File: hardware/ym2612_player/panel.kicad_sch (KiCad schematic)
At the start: 21 parts, among them J5 LCD (I2C backpack: GND, VCC, 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, Q1 BSS138, Q2 BSS138, SW1 Play (red cap), SW2 Stop, SW3 Left, SW4 Right, SW5 Edit, SW6 Exit, SW7 Write, SW8 Data knob

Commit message: Rev A PCB layout and PCBWay files
Board is 240 x 120 mm, 2 layers, placed by tools/layout.py and routed with
Freerouting (tools/route.py). DRC in KiCad 10: 0 errors, 0 unconnected,
matches the schematic. Adds Gerbers, BOM and placement (CPL) files for a
PCBWay turnkey order, and a top-view picture.

Also: volume slider moves off the board onto a 6-pin JST XH plug (J4), and
the Pico Plus 2 footprint now has its pads and outline in the right place.

Co-Authored-By: Claude Opus 5.5 (1M context) <noreply@anthropic.com>
Claude-Session: https://claude.ai/code/session_01JeM5NcWqyQVA3DixJkw6Wg
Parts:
- removed C38: 100nF, Capacitor_SMD:C_0603_1608Metric, symbol Device:C
- added SW1: Play (red cap), Button_Switch_THT:SW_PUSH-12mm, symbol Switch:SW_Push
- C35: renamed from R50; value 10k -> 10nF; footprint Resistor_SMD:R_0603_1608Metric -> Capacitor_SMD:C_0603_1608Metric; symbol Device:R -> Device:C; Spec 1%, 0603 -> X7R, 16V
- C37: renamed from J5; value LCD (I2C backpack: GND, VCC, SDA, SCL) -> 10uF; footprint Connector_JST:JST_XH_B4B-XH-A_1x04_P2.50mm_Vertical -> Capacitor_SMD:C_0805_2012Metric; symbol Connector_Generic:Conn_01x04 -> Device:C; MPN B4B-XH-A(LF)(SN) -> (none); Spec JST XH 4-pin header -> X5R, 10V, 0805
- C38: renamed from C37; value 10uF -> 100nF; footprint Capacitor_SMD:C_0805_2012Metric -> Capacitor_SMD:C_0603_1608Metric; Spec X5R, 10V, 0805 -> X7R, 16V
- J6: renamed from R54; value 4.7k -> LCD (I2C backpack: GND, VCC, SDA, SCL); footprint Resistor_SMD:R_0603_1608Metric -> Connector_JST:JST_XH_B4B-XH-A_1x04_P2.50mm_Vertical; symbol Device:R -> Connector_Generic:Conn_01x04; MPN (none) -> B4B-XH-A(LF)(SN); Spec 1%, 0603 -> JST XH 4-pin header
- Q1: renamed from C36; value 10nF -> BSS138; footprint Capacitor_SMD:C_0603_1608Metric -> Package_TO_SOT_SMD:SOT-23; symbol Device:C -> Transistor_FET:BSS138; MPN (none) -> BSS138; Spec X7R, 16V -> N-MOSFET, SOT-23
- Q2: renamed from R52; value 4.7k -> BSS138; footprint Resistor_SMD:R_0603_1608Metric -> Package_TO_SOT_SMD:SOT-23; symbol Device:R -> Transistor_FET:BSS138; MPN (none) -> BSS138; Spec 1%, 0603 -> N-MOSFET, SOT-23
- R49: renamed from SW8; value Data knob -> 10k; footprint Rotary_Encoder:RotaryEncoder_Alps_EC11E_Vertical_H20mm -> Resistor_SMD:R_0603_1608Metric; symbol Device:RotaryEncoder -> Device:R; MPN PEC11R-4215F-N0024 -> (none); Spec Bourns 24-step encoder, no push switch, 15 mm shaft (EC11 f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 -> 1%, 0603
- R51: renamed from Q1; value BSS138 -> 4.7k; footprint Package_TO_SOT_SMD:SOT-23 -> Resistor_SMD:R_0603_1608Metric; symbol Transistor_FET:BSS138 -> Device:R; MPN BSS138 -> (none); Spec N-MOSFET, SOT-23 -> 1%, 0603
- R53: renamed from Q2; value BSS138 -> 4.7k; footprint Package_TO_SOT_SMD:SOT-23 -> Resistor_SMD:R_0603_1608Metric; symbol Transistor_FET:BSS138 -> Device:R; MPN BSS138 -> (none); Spec N-MOSFET, SOT-23 -> 1%, 0603
- SW2: renamed from SW1; value Play (red cap) -> Stop
- SW3: renamed from SW2; value Stop -> Left
- SW4: renamed from SW3; value Left -> Right
- SW5: renamed from SW4; value Right -> Edit
- SW6: renamed from SW5; value Edit -> Exit
- SW7: renamed from SW6; value Exit -> Write
- SW8: renamed from SW7; value Write -> Data knob; footprint Button_Switch_THT:SW_PUSH-12mm -> Rotary_Encoder:RotaryEncoder_Alps_EC11E_Vertical_H20mm; symbol Switch:SW_Push -> Device:RotaryEncoder; MPN B3F-4055 -> PEC11R-4215F-N0024; Spec Omron 12 mm tactile switch, 7.3 mm tall, with a B32-series 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 -> Bourns 24-step encoder, no push switch, 15 mm shaft (EC11 f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
- renumbered C35 to C36, R49 to R50, R51 to R52, R53 to R54
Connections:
- net +3V3: now also Q1.1 (G), Q2.1 (G), R49.1; no longer C35.1, R52.1, R54.1
- net +5V: now also C37.1, J6.2 (Pin_2), R52.1, R54.1; no longer C37.2 (Pin_2), J6.1, Q2.1
- net BTN_EDIT: now also SW5.1; no longer SW6.1
- net BTN_EXIT: now also SW6.1; no longer SW7.1
- net BTN_LEFT: now also SW3.1; no longer SW4.1
- net BTN_PLAY: now also SW1.1; no longer SW2.1
- net BTN_RIGHT: now also SW4.1; no longer SW5.1
- net BTN_STOP: now also SW2.1; no longer SW3.1
- net BTN_WRITE: now also SW7.1; no longer SW8.1
- net ENC_A: now also C35.1, R49.2, SW8.A; no longer C36.1, R49.A, R50.2
- net ENC_B: now also C36.1, R50.2, SW8.B; no longer C35.2, Q1.1, R49.B
- net GND: now also C35.2, C37.2, J6.1 (Pin_1), SW8.C, SW1.2; no longer C37.1 (Pin_1), Q1.2, R49.C, SW8.2
- net I2C_SCL: now also Q2.2 (S); no longer R54.2
- net I2C_SDA: now also Q1.2 (S); no longer R52.2
- net LCD_SCL: now also J6.4 (Pin_4), Q2.3 (D), R54.2; no longer C37.4 (Pin_4), J6.2, R53.3 (D)
- net LCD_SDA: now also J6.3 (Pin_3), Q1.3 (D), R52.2; no longer C37.3 (Pin_3), Q2.2, R51.3 (D)
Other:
- moved on the sheet: C36, C38, R50, R52, R54, SW2, SW3, SW4, SW5, SW6, SW7

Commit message: Apply the Rev A fix register: decoupling, single ground, A.VCC filter, TPA6132A2
Schematic
- YM2612 A.VCC (pin 22) gets its own 10 ohm + 220 uF + 100 nF filter.
- /IC, A0, A1 pull-downs 10k -> 4.7k (RP2350 erratum E9).
- Headphone amp: NJM4556A replaced by a TPA6132A2 at -6 dB, no output caps,
  enabled by GP12 (HP_EN, 4.7k pull-down) so power-up doesn't pop.
- 47 uF electrolytic damps the L1/C4 resonance before the LP5907.
- GNDA merged into GND; NT1 removed. Four M3 holes for the LCD standoffs.
- Ferrite label 220R@100MHz to match BLM18PG221SN1D; C15/C22 spec X7R 50V;
  LED lead note for PCBWay.
- Pico Plus 2 and its headers marked do-not-fit (Joey supplies them);
  sockets are Sullins PPTC201LFBN-RC.

Layout
- Decoupling caps placed at the pin they serve (design.NEAR), 2-7 mm instead
  of 16-70 mm.
- One solid GND plane on both layers plus 332 stitching vias (tools/stitch.py).
- J6 moved out from under the LCD backpack; encoder moved below the LCD so
  the knob clears it.
- Re-routed with Freerouting; KiCad 7 DRC: 0 errors, 0 unconnected.

Co-Authored-By: Claude Opus 5.5 (1M context) <noreply@anthropic.com>
Claude-Session: https://claude.ai/code/session_01T6y8roX1LzS9uTuKVQBe9X
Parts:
- removed SW1: Play (red cap), Button_Switch_THT:SW_PUSH-12mm, symbol Switch:SW_Push
- removed SW2: Stop, Button_Switch_THT:SW_PUSH-12mm, symbol Switch:SW_Push
- added C41: 10uF, Capacitor_SMD:C_0805_2012Metric, symbol Device:C
- added C42: 100nF, Capacitor_SMD:C_0603_1608Metric, symbol Device:C
- C39: renamed from Q1; value BSS138 -> 10nF; footprint Package_TO_SOT_SMD:SOT-23 -> Capacitor_SMD:C_0603_1608Metric; symbol Transistor_FET:BSS138 -> Device:C; MPN BSS138 -> (none); Spec N-MOSFET, SOT-23 -> X7R, 16V
- C40: renamed from R51; value 4.7k -> 10nF; footprint Resistor_SMD:R_0603_1608Metric -> Capacitor_SMD:C_0603_1608Metric; symbol Device:R -> Device:C; Spec 1%, 0603 -> X7R, 16V
- J6: renamed from C38; value 100nF -> LCD (I2C backpack: GND, VCC, SDA, SCL); footprint Capacitor_SMD:C_0603_1608Metric -> Connector_JST:JST_XH_B4B-XH-A_1x04_P2.50mm_Vertical; symbol Device:C -> Connector_Generic:Conn_01x04; MPN (none) -> B4B-XH-A(LF)(SN); Spec X7R, 16V -> JST XH 4-pin header
- Q1: renamed from R52; value 4.7k -> BSS138; footprint Resistor_SMD:R_0603_1608Metric -> Package_TO_SOT_SMD:SOT-23; symbol Device:R -> Transistor_FET:BSS138; MPN (none) -> BSS138; Spec 1%, 0603 -> N-MOSFET, SOT-23
- Q2: renamed from R54; value 4.7k -> BSS138; footprint Resistor_SMD:R_0603_1608Metric -> Package_TO_SOT_SMD:SOT-23; symbol Device:R -> Transistor_FET:BSS138; MPN (none) -> BSS138; Spec 1%, 0603 -> N-MOSFET, SOT-23
- R45: renamed from C35; value 10nF -> 10k; footprint Capacitor_SMD:C_0603_1608Metric -> Resistor_SMD:R_0603_1608Metric; symbol Device:C -> Device:R; Spec X7R, 16V -> 1%, 0603
- R46: renamed from C36; value 10nF -> 10k; footprint Capacitor_SMD:C_0603_1608Metric -> Resistor_SMD:R_0603_1608Metric; symbol Device:C -> Device:R; Spec X7R, 16V -> 1%, 0603
- R47: renamed from Q2; value BSS138 -> 4.7k; footprint Package_TO_SOT_SMD:SOT-23 -> Resistor_SMD:R_0603_1608Metric; symbol Transistor_FET:BSS138 -> Device:R; MPN BSS138 -> (none); Spec N-MOSFET, SOT-23 -> 1%, 0603
- R49: renamed from J6; value LCD (I2C backpack: GND, VCC, SDA, SCL) -> 4.7k; footprint Connector_JST:JST_XH_B4B-XH-A_1x04_P2.50mm_Vertical -> Resistor_SMD:R_0603_1608Metric; symbol Connector_Generic:Conn_01x04 -> Device:R; MPN B4B-XH-A(LF)(SN) -> (none); Spec JST XH 4-pin header -> 1%, 0603
- R50: renamed from C37; value 10uF -> 4.7k; footprint Capacitor_SMD:C_0805_2012Metric -> Resistor_SMD:R_0603_1608Metric; symbol Device:C -> Device:R; Spec X5R, 10V, 0805 -> 1%, 0603
- SW1: renamed from SW3; value Left -> Play (red cap)
- SW2: renamed from SW4; value Right -> Stop
- SW3: renamed from SW5; value Edit -> Left
- SW4: renamed from SW6; value Exit -> Right
- SW5: renamed from SW7; value Write -> Edit
- SW6: renamed from SW8; value Data knob -> Exit; footprint Rotary_Encoder:RotaryEncoder_Alps_EC11E_Vertical_H20mm -> Button_Switch_THT:SW_PUSH-12mm; symbol Device:RotaryEncoder -> Switch:SW_Push; MPN PEC11R-4215F-N0024 -> B3F-4055; Spec Bourns 24-step encoder, no push switch, 15 mm shaft (EC11 f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 -> Omron 12 mm tactile switch, 7.3 mm tall, with a B32-series 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
- SW7: renamed from R49; value 10k -> Write; footprint Resistor_SMD:R_0603_1608Metric -> Button_Switch_THT:SW_PUSH-12mm; symbol Device:R -> Switch:SW_Push; MPN (none) -> B3F-4055; Spec 1%, 0603 -> Omron 12 mm tactile switch, 7.3 mm tall, with a B32-series 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
- SW8: renamed from R50; value 10k -> Data knob; footprint Resistor_SMD:R_0603_1608Metric -> Rotary_Encoder:RotaryEncoder_Alps_EC11E_Vertical_H20mm; symbol Device:R -> Device:RotaryEncoder; MPN (none) -> PEC11R-4215F-N0024; Spec 1%, 0603 -> Bourns 24-step encoder, no push switch, 15 mm shaft (EC11 f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
- renumbered R53 to R48
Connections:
- net +3V3: now also Q1.1 (G), Q2.1 (G), R45.1, R46.1, R49.1; no longer C39.1 (G), C40.1, R48.1, SW7.1, SW8.1
- net +5V: now also J6.2 (Pin_2), R48.1, C41.1, C42.1; no longer J6.1, Q1.1, Q2.1, R49.2 (Pin_2)
- net BTN_EDIT: now also SW5.1; no longer SW3.1
- net BTN_EXIT: now also SW6.1; no longer SW4.1
- net BTN_LEFT: now also SW3.1; no longer SW1.1
- net BTN_PLAY: now also SW1.1
- net BTN_RIGHT: now also SW4.1; no longer SW2.1
- net BTN_STOP: now also SW2.1
- net BTN_WRITE: now also SW7.1; no longer SW5.1
- net ENC_A: now also C39.1, R45.2, SW8.A; no longer R45.1, SW6.A, SW7.2
- net ENC_B: now also C40.1, R46.2, SW8.B; no longer R46.1, SW6.B, SW8.2
- net GND: now also C39.2, C40.2, J6.1 (Pin_1), SW6.2, SW7.2, SW8.C, C41.2, C42.2; no longer J6.2, R45.2, R46.2, R49.1 (Pin_1), R50.2, SW6.C
- net I2C_SCL: now also Q2.2 (S), R49.2; no longer R47.2 (S), R48.2
- net I2C_SDA: now also Q1.2 (S), R47.2; no longer C39.2 (S), C40.2
- net LCD_SCL: now also J6.4 (Pin_4), Q2.3 (D), R50.2; no longer Q2.2, R47.3 (D), R49.4 (Pin_4)
- net LCD_SDA: now also J6.3 (Pin_3), Q1.3 (D), R48.2; no longer C39.3 (D), Q1.2, R49.3 (Pin_3)
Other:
- moved on the sheet: R48, SW1, SW2, SW3, SW4, SW5

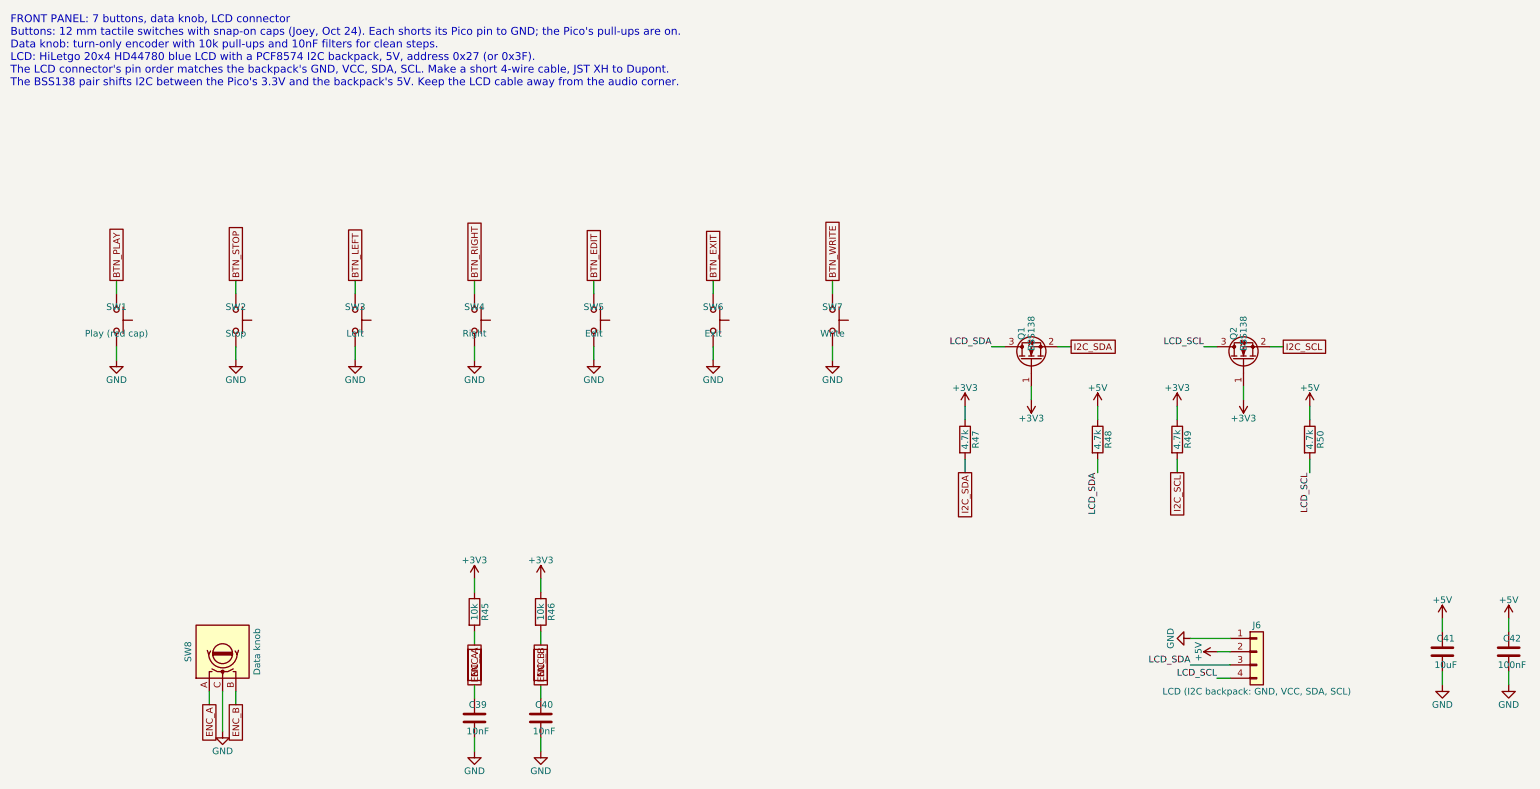
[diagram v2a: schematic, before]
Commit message: Schematic: draw real wires between parts instead of name tags
tools/wires.py routes each page's nets on the 1.27 mm grid around part bodies and text.
Power pins keep power symbols (neighbouring pins share one), signals that leave a page get
one global label, and the netlist check still matches design.py exactly (0 mismatches).
Sound chip and audio pages re-laid out so the wiring reads left to right; title blocks say Rev B.

Co-Authored-By: Claude Opus 5.5 <noreply@anthropic.com>
Claude-Session: https://claude.ai/code/session_01TDTDVidYRoyJdUGgsyVTSw
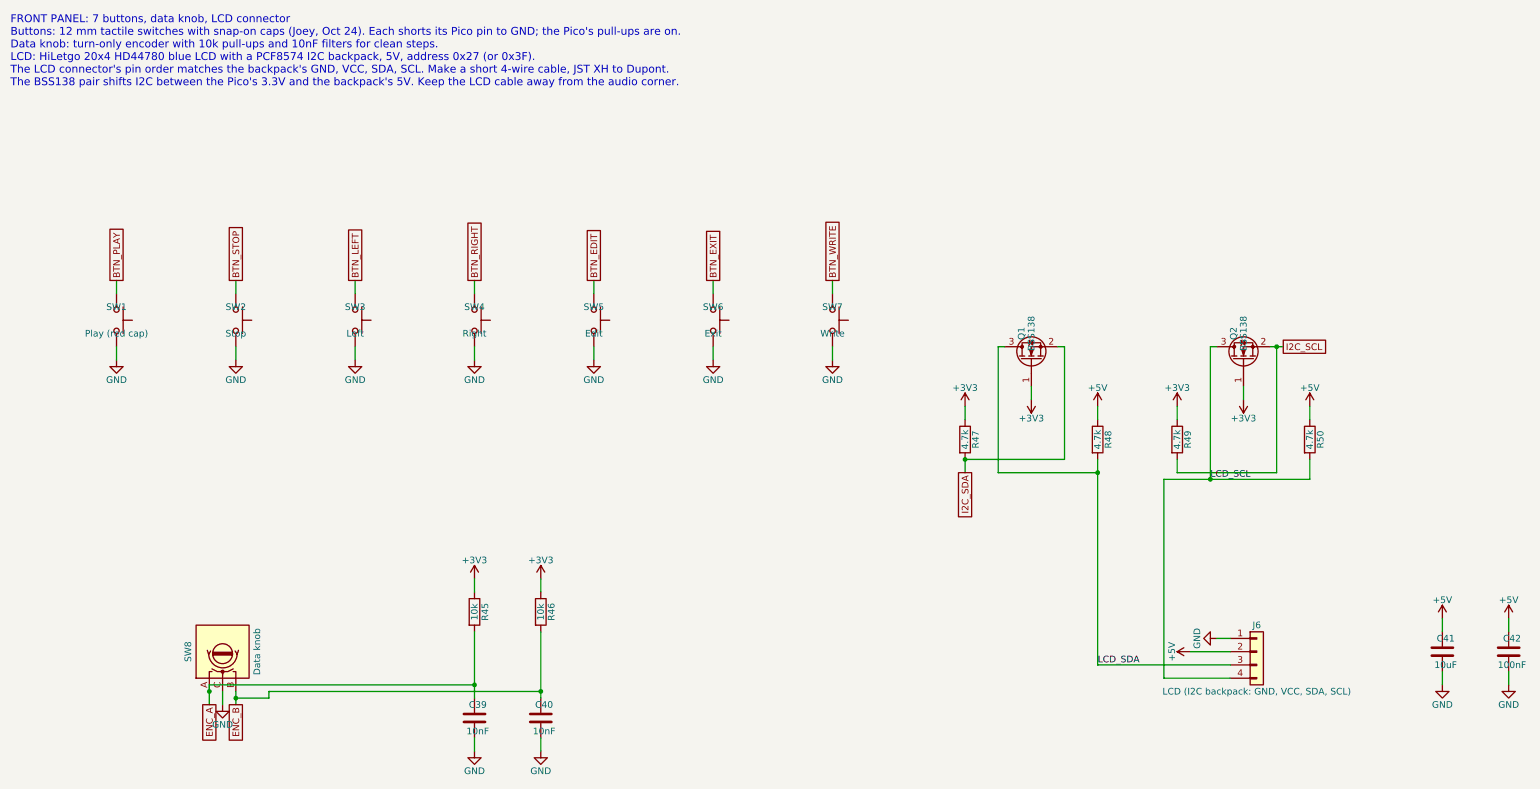
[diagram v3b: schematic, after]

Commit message: Schematic: PWR_FLAG on YM_AVCC (KiCad 10 ERC: A.VCC is fed through R21)
Co-Authored-By: Claude Opus 5.5 <noreply@anthropic.com>
Claude-Session: https://claude.ai/code/session_01TDTDVidYRoyJdUGgsyVTSw
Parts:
- removed SW1: Play (red cap), Button_Switch_THT:SW_PUSH-12mm, symbol Switch:SW_Push
- added C42: 100nF, Capacitor_SMD:C_0603_1608Metric, symbol Device:C
- C40: renamed from Q1; value BSS138 -> 10nF; footprint Package_TO_SOT_SMD:SOT-23 -> Capacitor_SMD:C_0603_1608Metric; symbol Transistor_FET:BSS138 -> Device:C; MPN BSS138 -> (none); Spec N-MOSFET, SOT-23 -> X7R, 16V
- C41: renamed from C42; value 100nF -> 10uF; footprint Capacitor_SMD:C_0603_1608Metric -> Capacitor_SMD:C_0805_2012Metric; Spec X7R, 16V -> X5R, 10V, 0805
- J6: renamed from C41; value 10uF -> LCD (I2C backpack: GND, VCC, SDA, SCL); footprint Capacitor_SMD:C_0805_2012Metric -> Connector_JST:JST_XH_B4B-XH-A_1x04_P2.50mm_Vertical; symbol Device:C -> Connector_Generic:Conn_01x04; MPN (none) -> B4B-XH-A(LF)(SN); Spec X5R, 10V, 0805 -> JST XH 4-pin header
- Q1: renamed from R47; value 4.7k -> BSS138; footprint Resistor_SMD:R_0603_1608Metric -> Package_TO_SOT_SMD:SOT-23; symbol Device:R -> Transistor_FET:BSS138; MPN (none) -> BSS138; Spec 1%, 0603 -> N-MOSFET, SOT-23
- Q2: renamed from R49; value 4.7k -> BSS138; footprint Resistor_SMD:R_0603_1608Metric -> Package_TO_SOT_SMD:SOT-23; symbol Device:R -> Transistor_FET:BSS138; MPN (none) -> BSS138; Spec 1%, 0603 -> N-MOSFET, SOT-23
- R46: renamed from C39; value 10nF -> 10k; footprint Capacitor_SMD:C_0603_1608Metric -> Resistor_SMD:R_0603_1608Metric; symbol Device:C -> Device:R; Spec X7R, 16V -> 1%, 0603
- R48: renamed from Q2; value BSS138 -> 4.7k; footprint Package_TO_SOT_SMD:SOT-23 -> Resistor_SMD:R_0603_1608Metric; symbol Transistor_FET:BSS138 -> Device:R; MPN BSS138 -> (none); Spec N-MOSFET, SOT-23 -> 1%, 0603
- R50: renamed from J6; value LCD (I2C backpack: GND, VCC, SDA, SCL) -> 4.7k; footprint Connector_JST:JST_XH_B4B-XH-A_1x04_P2.50mm_Vertical -> Resistor_SMD:R_0603_1608Metric; symbol Connector_Generic:Conn_01x04 -> Device:R; MPN B4B-XH-A(LF)(SN) -> (none); Spec JST XH 4-pin header -> 1%, 0603
- SW1: renamed from SW2; value Stop -> Play (red cap)
- SW2: renamed from SW3; value Left -> Stop
- SW3: renamed from SW4; value Right -> Left
- SW4: renamed from SW5; value Edit -> Right
- SW5: renamed from SW6; value Exit -> Edit
- SW6: renamed from SW7; value Write -> Exit
- SW7: renamed from SW8; value Data knob -> Write; footprint Rotary_Encoder:RotaryEncoder_Alps_EC11E_Vertical_H20mm -> Button_Switch_THT:SW_PUSH-12mm; symbol Device:RotaryEncoder -> Switch:SW_Push; MPN PEC11R-4215F-N0024 -> B3F-4055; Spec Bourns 24-step encoder, no push switch, 15 mm shaft (EC11 f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 -> Omron 12 mm tactile switch, 7.3 mm tall, with a B32-series 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
- SW8: renamed from R45; value 10k -> Data knob; footprint Resistor_SMD:R_0603_1608Metric -> Rotary_Encoder:RotaryEncoder_Alps_EC11E_Vertical_H20mm; symbol Device:R -> Device:RotaryEncoder; MPN (none) -> PEC11R-4215F-N0024; Spec 1%, 0603 -> Bourns 24-step encoder, no push switch, 15 mm shaft (EC11 f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
- renumbered C40 to C39, R46 to R45, R48 to R47, R50 to R49
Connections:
- net +3V3: now also R46.1, R47.1, R49.1; no longer C40.1 (G), R48.1 (G), SW8.1
- net +5V: now also J6.2 (Pin_2), R48.1, R50.1, C42.1; no longer J6.1, R47.1, R49.1, R50.2 (Pin_2)
- net BTN_EDIT: now also SW5.1; no longer SW4.1
- net BTN_EXIT: now also SW6.1; no longer SW5.1
- net BTN_LEFT: now also SW3.1; no longer SW2.1
- net BTN_PLAY: now also SW1.1
- net BTN_RIGHT: now also SW4.1; no longer SW3.1
- net BTN_STOP: now also SW2.1; no longer SW1.1
- net BTN_WRITE: now also SW7.1; no longer SW6.1
- net ENC_A: now also C39.1, R45.2, SW8.A; no longer R46.1, SW7.A, SW8.2
- net ENC_B: now also C40.1, R46.2, SW8.B; no longer C39.1, R45.2, SW7.B
- net GND: now also C40.2, J6.1 (Pin_1), SW7.2, SW8.C, C42.2; no longer J6.2, R46.2, R50.1 (Pin_1), SW7.C
- net I2C_SCL: now also R49.2; no longer R48.2 (S)
- net I2C_SDA: now also R47.2; no longer C40.2 (S)
- net LCD_SCL: now also J6.4 (Pin_4), Q2.3 (D), R50.2; no longer R48.3 (D), R49.2, R50.4 (Pin_4)
- net LCD_SDA: now also J6.3 (Pin_3), Q1.3 (D), R48.2; no longer C40.3 (D), R47.2, R50.3 (Pin_3)
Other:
- moved on the sheet: C39, C41, R45, R47, R49, SW1, SW2, SW3, SW4, SW5, SW6
